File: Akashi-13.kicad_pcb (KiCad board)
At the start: 4 copper layers, 67.3 x 91.4 mm, 38 parts, among them J1 Conn_02x35_Odd_Even, J2 Conn_02x35_Odd_Even, J3 CONN12_011D01BNL_PUL, U1 LAN9220-ABZJ, U2 93AA46AT-IOT, X1 DFA-S15

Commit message: Add vias to the exposed pad of U1.
Also following FusionPCB rules.
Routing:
- net GND: vias 11 -> 17
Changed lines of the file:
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@@
     (pad_to_mask_clearance 0)
     (pcbplotparams
-      (layerselection 0x00010fc_ffffffff)
+      (layerselection 0x00010f0_ffffffff)
       (plot_on_all_layers_selection 0x0000000_00000000)
       (disableapertmacros false)
       (usegerberextensions false)
-      (usegerberattributes true)
-      (usegerberadvancedattributes true)
+      (usegerberattributes false)
+      (usegerberadvancedattributes false)
       (creategerberjobfile true)
       (dashed_line_dash_ratio 12.000000)
@@
   (gr_line (start 151.13 77.47) (end 111.76 77.47)
     (stroke (width 0.1) (type default)) (layer "Edge.Cuts"))
-  (gr_text "(C) Seiichi Horie, 2023\nhttps://github.com/suikan4github/Akashi-13" (at 148.59 90.17) (layer "F.SilkS")
+  (gr_text "(C) Seiichi Horie, 2023\nhttps://github.com/suikan4github/Akashi-13" (at 148.59 90.17) (layer "B.SilkS")
     (effects (font (size 1 1) (thickness 0.15)) (justify left bottom mirror))
   )
@@
   (via blind (at 125.9942 118.747) (size 0.6) (drill 0.2) (layers "F.Cu" "B.Cu") (net 16))
   (via (at 137.5 107.25) (size 0.5) (drill 0.2) (layers "F.Cu" "B.Cu") (net 16))
+  (via locked (at 134 111) (size 0.8) (drill 0.4) (layers "F.Cu" "B.Cu") (net 16))
+  (via locked (at 132 111) (size 0.8) (drill 0.4) (layers "F.Cu" "B.Cu") (net 16))
   (via blind (at 123.5235 121.3776) (size 0.6) (drill 0.2) (layers "F.Cu" "B.Cu") (net 16))
+  (via locked (at 130 111) (size 0.8) (drill 0.4) (layers "F.Cu" "B.Cu") (net 16))
   (via blind (at 136.8802 102.4141) (size 0.6) (drill 0.2) (layers "F.Cu" "B.Cu") (net 16))
   (via blind (at 120.3581 129.1241) (size 0.6) (drill 0.2) (layers "F.Cu" "B.Cu") (net 16))
+  (via locked (at 134 109) (size 0.8) (drill 0.4) (layers "F.Cu" "B.Cu") (net 16))
   (via blind (at 138.171 120.3402) (size 0.6) (drill 0.2) (layers "F.Cu" "B.Cu") (net 16))
   (via (at 136.75 107.01) (size 0.5) (drill 0.2) (layers "F.Cu" "B.Cu") (net 16))
+  (via locked (at 130 109) (size 0.8) (drill 0.4) (layers "F.Cu" "B.Cu") (net 16))
   (via blind (at 123.7602 112.1073) (size 0.6) (drill 0.2) (layers "F.Cu" "B.Cu") (net 16))
   (via blind (at 124.6845 113.5878) (size 0.6) (drill 0.2) (layers "F.Cu" "B.Cu") (net 16))
   (via blind (at 115.1363 114.8908) (size 0.6) (drill 0.2) (layers "F.Cu" "B.Cu") (net 16))
+  (via locked (at 132 109) (size 0.8) (drill 0.4) (layers "F.Cu" "B.Cu") (net 16))
   (segment (start 135.775 131) (end 134.9674 130.1924) (width 0.25) (layer "B.Cu") (net 16))
   (segment (start 119.3918 108.7942) (end 123.1153 108.7942) (width 0.25) (layer "B.Cu") (net 16))

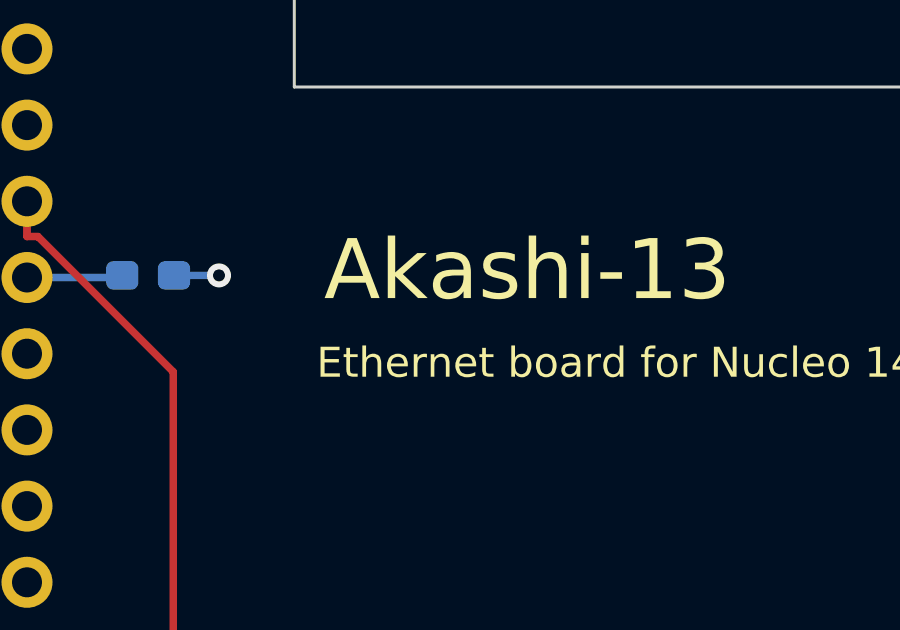
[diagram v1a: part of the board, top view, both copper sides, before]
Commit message: Add version number to sylkscreen
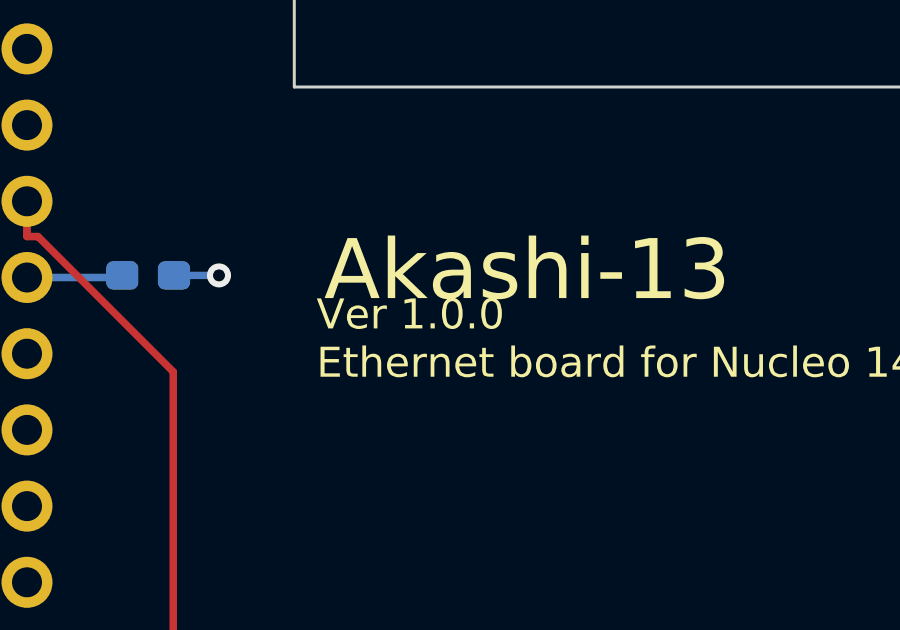
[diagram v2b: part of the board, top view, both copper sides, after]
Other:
- board text added: "Ver 1.0.0 Ethernet board for Nucleo 144"
- board text removed: "Ethernet board for Nucleo 144"
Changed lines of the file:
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@@
     (effects (font (size 1 1) (thickness 0.15)) (justify left bottom))
   )
-  (gr_text "Ethernet board for Nucleo 144" (at 112.5 87.25) (layer "F.SilkS")
+  (gr_text "Ver 1.0.0\nEthernet board for Nucleo 144" (at 112.5 87.25) (layer "F.SilkS")
     (effects (font (size 1 1) (thickness 0.15)) (justify left bottom))
   )
